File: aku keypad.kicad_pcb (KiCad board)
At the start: 2 copper layers, 47.6 x 46 mm, 19 parts, among them J1 USB_C_Receptacle_USB2.0, SW1 SW_Push, SW2 MX_SW_HS, SW3 MX_SW_HS, U1 SRV05-4, U2 ATmega32U2-M, Y1 Crystal_GND24_Small

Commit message: Added front ground fill
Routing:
- added copper zone on F.Cu, net GND
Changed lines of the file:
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@@
   (segment (start 47.7525 78.10125) (end 48.9025 76.95125) (width 0.25) (layer "B.Cu") (net 38))
   (segment (start 53.308597 72.549493) (end 52.851574 73.006516) (width 0.25) (layer "B.Cu") (net 38))
+  (zone (net 1) (net_name "GND") (layer "F.Cu") (hatch edge 0.508)
+    (connect_pads (clearance 0.508))
+    (min_thickness 0.254) (filled_areas_thickness no)
+    (fill yes (thermal_gap 0.508) (thermal_bridge_width 0.508))
+    (polygon
+      (pts
+        (xy 61.11875 39.6875)
+        (xy 79.375 39.6875)
+        (xy 79.375 78.58125)
+        (xy 31.75 78.58125)
+        (xy 31.75 39.6875)
+        (xy 50.00625 39.6875)
+        (xy 50.00625 32.54375)
+        (xy 61.11875 32.54375)
+      )
+    )
+  )
   (zone (net 1) (net_name "GND") (layer "B.Cu") (hatch edge 0.508)
     (connect_pads yes (clearance 0.508))

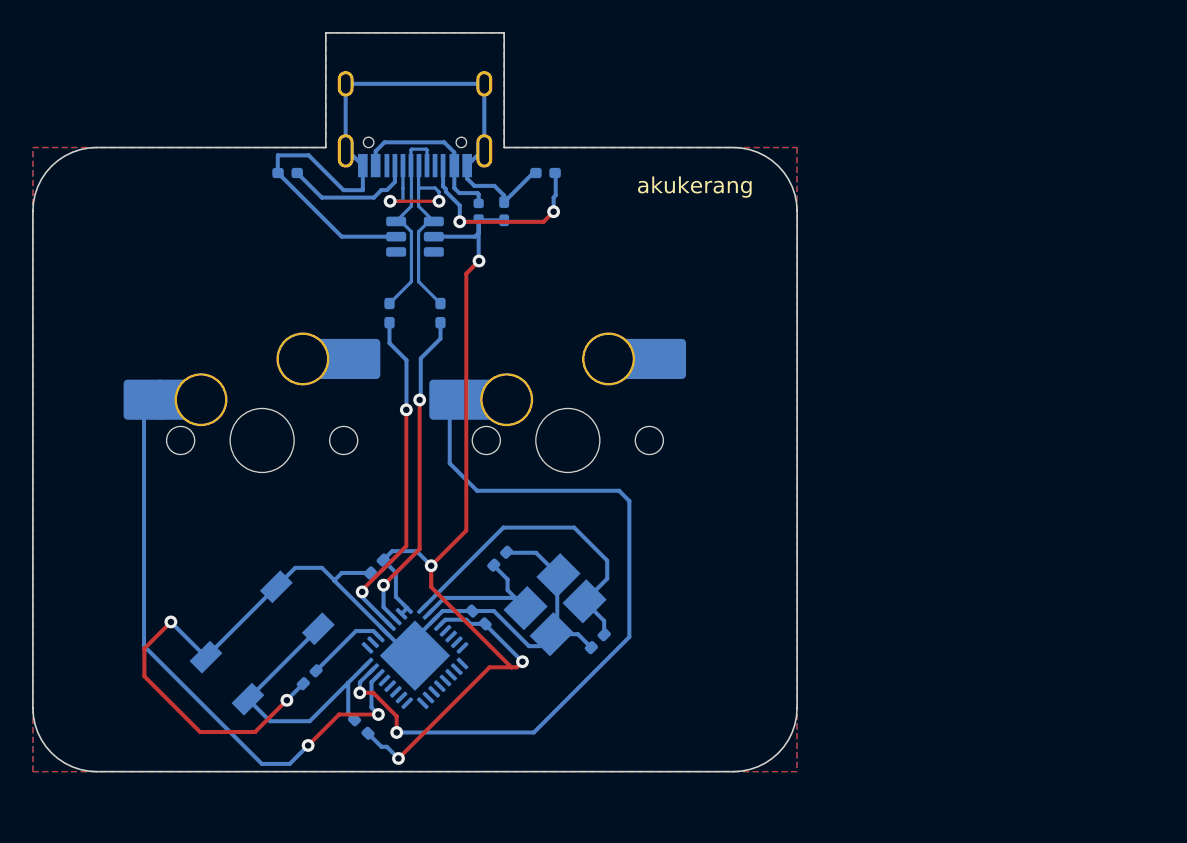
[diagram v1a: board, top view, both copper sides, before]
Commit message: redid routing on pcb
added type-c submodule, redid routing, changed usb components
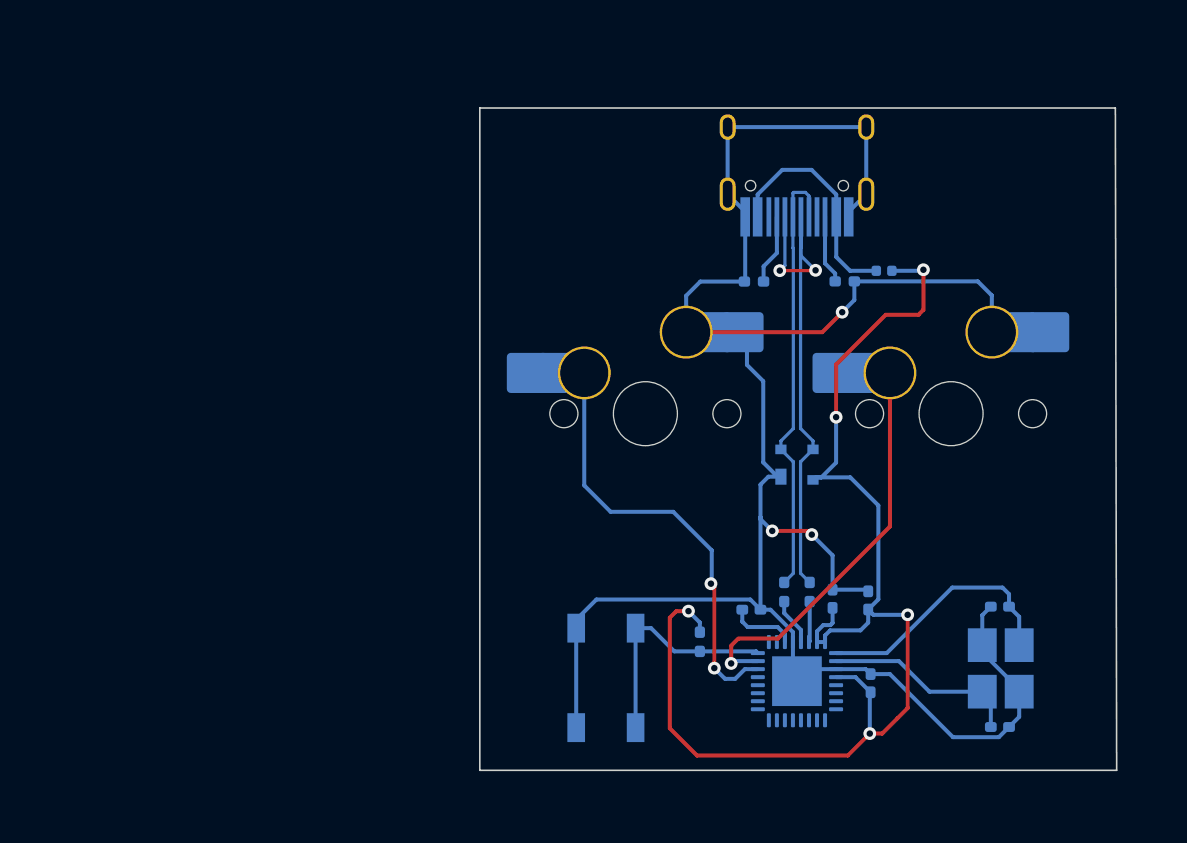
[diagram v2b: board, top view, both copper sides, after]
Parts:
- removed J1: USB_C_Receptacle_USB2.0, Connector_USB:USB_C_Receptacle_HRO_TYPE-C-31-M-12
- removed U1: SRV05-4, marbastlib-various:SOT-23-6-routable
- added D1: PRTR5V0U2X, Package_TO_SOT_SMD:SOT-143, B.Cu at (79.4, 59.5)
- added USB1: HRO-TYPE-C-31-M-12, Type-C:HRO-TYPE-C-31-M-12-HandSoldering, B.Cu at (79.4, 35.8)
- moved C6 37.2 mm to (84.0, 73.1)
- moved C2 32.9 mm to (92.0, 75.8), turned to 180 degrees
- moved R4 30.1 mm to (78.6, 67.4)
- moved R2 29.8 mm to (76.7, 48.0)
- moved R5 28.8 mm to (80.2, 67.4)
- moved C5 28.5 mm to (81.6, 67.8), turned to 90 degrees
- moved Y1 28.1 mm to (92.1, 72.2), turned to -90 degrees
- moved C3 27.8 mm to (76.5, 68.5), turned to 180 degrees
- moved F1 25.5 mm to (84.8, 47.4), turned to 0 degrees
- moved C1 25.2 mm to (92.0, 68.3), turned to 0 degrees
- moved C4 24.3 mm to (83.8, 67.9), turned to 90 degrees
- moved SW3 23.9 mm to (69.9, 56.3)
- moved SW2 23.9 mm to (89.0, 56.3)
- moved U2 23.9 mm to (79.4, 72.9), turned to 180 degrees
- moved R1 21.8 mm to (73.3, 70.5), turned to -90 degrees
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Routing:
- net GND: track 109.8 -> 140.5 mm, vias 2 -> 3
- net COL1: track 47.3 -> 28.9 mm, vias 2 -> 1
- net Net-(R4-Pad2): track 21.2 -> 2.95 mm, vias 2 -> 0
- net Net-(R5-Pad2): track 20.3 -> 2.54 mm, vias 2 -> 0
- net D-: track 17.4 -> 33.1 mm
- net D+: track 12.4 -> 27.6 mm
- net +5V: track 63.5 -> 78.1 mm, vias 4 -> 5
- net Net-(R3-Pad1): track 12.5 -> 4.28 mm, vias 2 -> 0
- net COL0: track 37.1 -> 30.9 mm
- net XTAL1: track 20.1 -> 16.1 mm
- net Net-(R2-Pad1): track 8.15 -> 4.37 mm
- net Net-(R1-Pad2): track 18.2 -> 14.5 mm
- net VCC: track 10.8 -> 14.3 mm
- net XTAL2: track 10.2 -> 12.3 mm
- net Net-(C3-Pad2): track 5.07 -> 4.21 mm
- removed copper zone on B.Cu, net GND
- removed copper zone on F.Cu, net GND
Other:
- board size 47.6 x 46 mm -> 39.7 x 41.3 mm
- board text removed: "akukerang"

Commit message: Added mounting holes
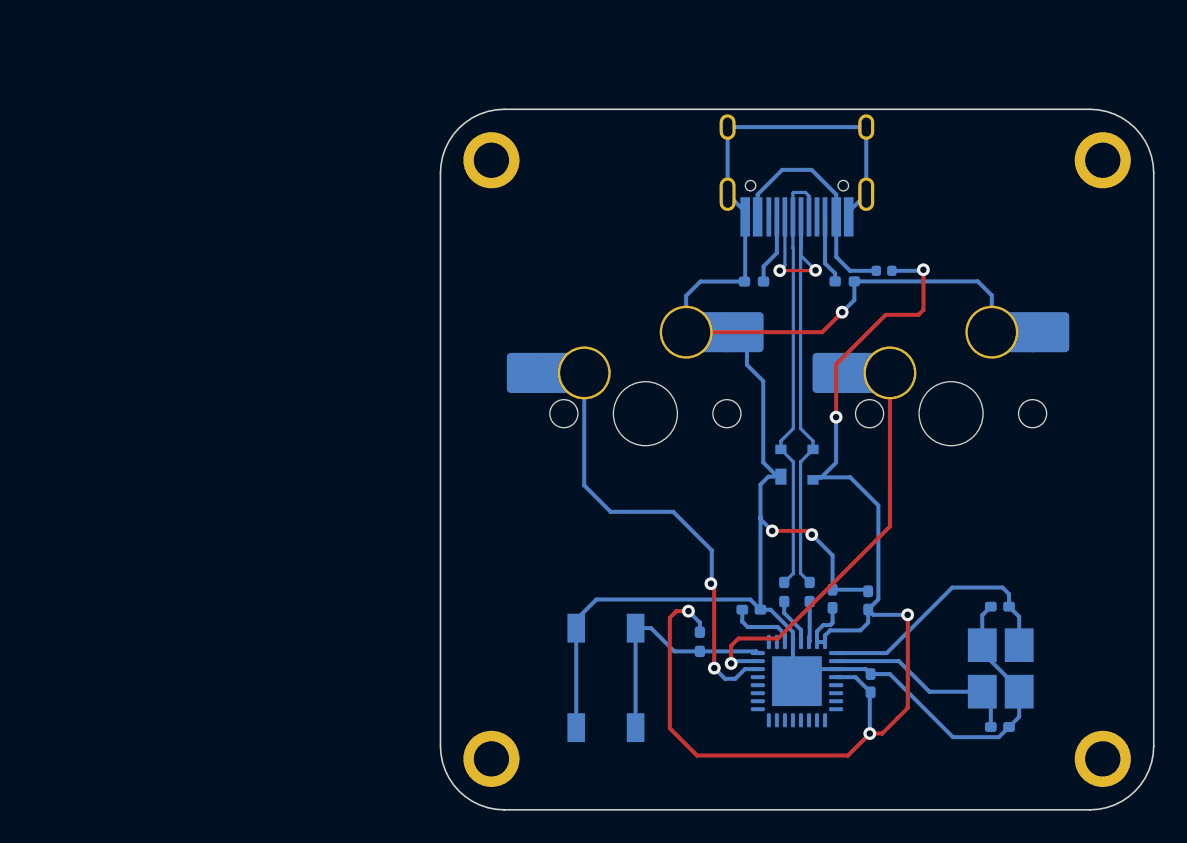
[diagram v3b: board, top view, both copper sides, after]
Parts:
- added H1: MountingHole, random-keyboard-parts:Generic-Mounthole, F.Cu at (60.3, 40.5)
- added H2: MountingHole, random-keyboard-parts:Generic-Mounthole, F.Cu at (98.4, 40.5)
- added H3: MountingHole, random-keyboard-parts:Generic-Mounthole, F.Cu at (60.3, 77.8)
- added H4: MountingHole, random-keyboard-parts:Generic-Mounthole, F.Cu at (98.4, 77.8)
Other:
- board size 39.7 x 41.3 mm -> 44.4 x 43.7 mm
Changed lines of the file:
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@@
   (net 35 "COL1")
   (net 36 "COL0")
+  (footprint "random-keyboard-parts:Generic-Mounthole" (layer "F.Cu")
+    (at 98.425 40.48125)
+    (property "Sheetfile" "aku keypad.kicad_sch")
+    (property "Sheetname" "")
+    (attr exclude_from_pos_files)
+    (fp_text reference "H2" (at 0 2) (layer "Dwgs.User")
+      (effects (font (size 1 1) (thickness 0.15)))
+    )
+    (fp_text value "MountingHole" (at 0 -2) (layer "Dwgs.User")
+      (effects (font (size 1 1) (thickness 0.15)))
+    )
+    (pad "1" thru_hole circle locked (at 0 0) (size 3.5 3.5) (drill 2.2) (layers *.Cu *.Mask))
+  )
+  (footprint "random-keyboard-parts:Generic-Mounthole" (layer "F.Cu")
+    (at 60.325 77.7875)
+    (property "Sheetfile" "aku keypad.kicad_sch")
+    (property "Sheetname" "")
+    (attr exclude_from_pos_files)
+    (fp_text reference "H3" (at 0 2) (layer "Dwgs.User")
+      (effects (font (size 1 1) (thickness 0.15)))
+    )
+    (fp_text value "MountingHole" (at 0 -2) (layer "Dwgs.User")
+      (effects (font (size 1 1) (thickness 0.15)))
+    )
+    (pad "1" thru_hole circle locked (at 0 0) (size 3.5 3.5) (drill 2.2) (layers *.Cu *.Mask))
+  )
+  (footprint "random-keyboard-parts:Generic-Mounthole" (layer "F.Cu")
+    (at 60.325 40.48125)
+    (property "Sheetfile" "aku keypad.kicad_sch")
+    (property "Sheetname" "")
+    (attr exclude_from_pos_files)
+    (fp_text reference "H1" (at 0 2) (layer "Dwgs.User")
+      (effects (font (size 1 1) (thickness 0.15)))
+    )
+    (fp_text value "MountingHole" (at 0 -2) (layer "Dwgs.User")
+      (effects (font (size 1 1) (thickness 0.15)))
+    )
+    (pad "1" thru_hole circle locked (at 0 0) (size 3.5 3.5) (drill 2.2) (layers *.Cu *.Mask))
+  )
+  (footprint "random-keyboard-parts:Generic-Mounthole" (layer "F.Cu")
+    (at 98.425 77.7875)
+    (property "Sheetfile" "aku keypad.kicad_sch")
+    (property "Sheetname" "")
+    (attr exclude_from_pos_files)
+    (fp_text reference "H4" (at 0 2) (layer "Dwgs.User")
+      (effects (font (size 1 1) (thickness 0.15)))
+    )
+    (fp_text value "MountingHole" (at 0 -2) (layer "Dwgs.User")
+      (effects (font (size 1 1) (thickness 0.15)))
+    )
+    (pad "1" thru_hole circle locked (at 0 0) (size 3.5 3.5) (drill 2.2) (layers *.Cu *.Mask))
+  )
   (footprint "Button_Switch_SMD:SW_SPST_SKQG_WithStem" (layer "B.Cu")
     (at 67.459644 72.74 -90)
@@
     )
   )
-  (gr_line (start 99.209644 37.225) (end 59.6025 37.225) (layer "Edge.Cuts") (width 0.1))
-  (gr_line (start 59.6025 78.5) (end 59.6025 37.225) (layer "Edge.Cuts") (width 0.1))
-  (gr_line (start 99.29 78.5) (end 59.6025 78.5) (layer "Edge.Cuts") (width 0.1))
-  (gr_line (start 99.29 78.5) (end 99.209644 37.225) (layer "Edge.Cuts") (width 0.1))
+  (gr_arc (start 61.11875 80.9625) (mid 58.31242 79.80008) (end 57.15 76.99375) (layer "Edge.Cuts") (width 0.1))
+  (gr_line (start 61.11875 37.30625) (end 97.63125 37.30625) (layer "Edge.Cuts") (width 0.1))
+  (gr_line (start 61.11875 80.9625) (end 97.63125 80.9625) (layer "Edge.Cuts") (width 0.1))
+  (gr_arc (start 97.63125 37.30625) (mid 100.43758 38.46867) (end 101.6 41.275) (layer "Edge.Cuts") (width 0.1))
+  (gr_line (start 57.15 41.275) (end 57.15 76.99375) (layer "Edge.Cuts") (width 0.1))
+  (gr_arc (start 101.6 76.99375) (mid 100.43758 79.80008) (end 97.63125 80.9625) (layer "Edge.Cuts") (width 0.1))
+  (gr_line (start 101.6 76.99375) (end 101.6 41.275) (layer "Edge.Cuts") (width 0.1))
+  (gr_arc (start 57.15 41.275) (mid 58.31242 38.46867) (end 61.11875 37.30625) (layer "Edge.Cuts") (width 0.1))
   (segment (start 82.185894 49.95) (end 80.940894 51.195) (width 0.25) (layer "F.Cu") (net 1))
   (segment (start 80.940894 51.195) (end 72.46125 51.195) (width 0.25) (layer "F.Cu") (net 1))

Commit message: more rerouting, added edge cuts around usb
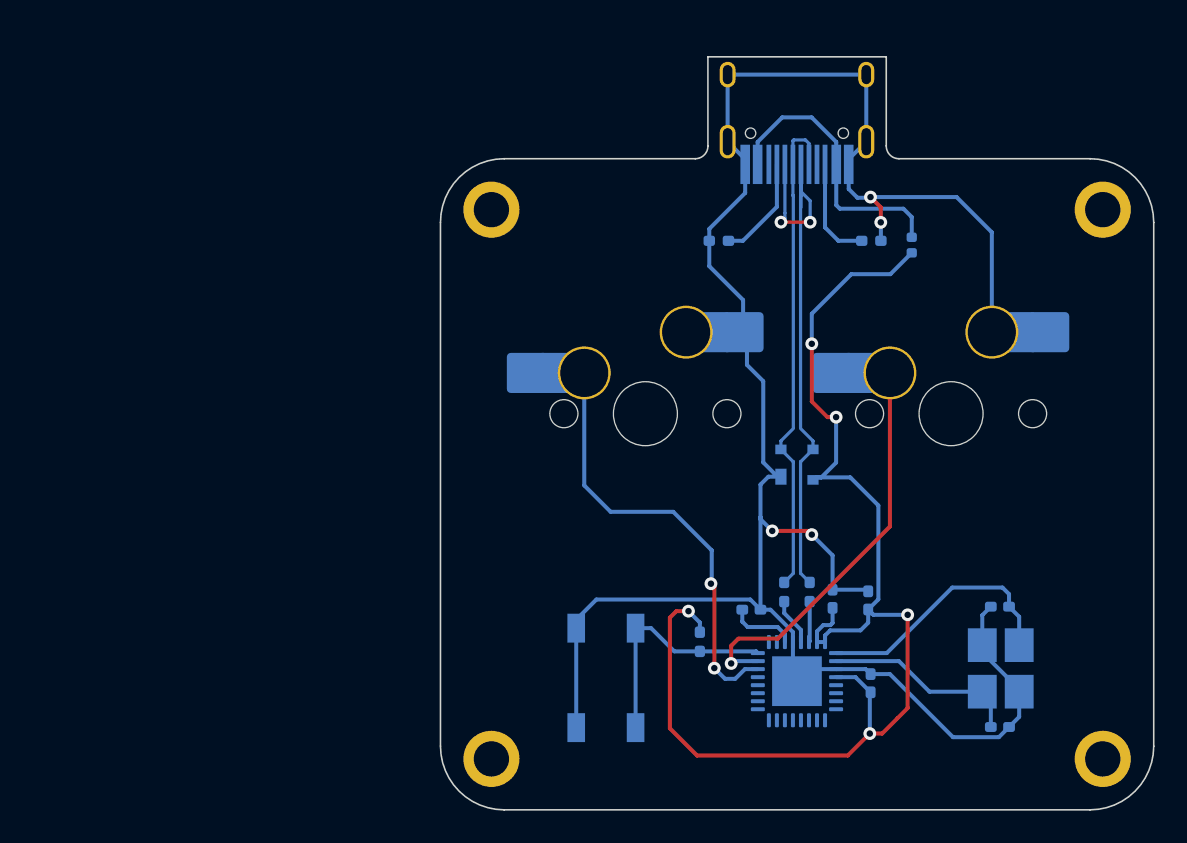
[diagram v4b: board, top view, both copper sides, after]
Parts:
- moved R2 3.35 mm to (74.5, 45.5)
- moved USB1 3.27 mm to (79.4, 32.5)
- moved H1 3.08 mm to (60.3, 43.6)
- moved H2 3.08 mm to (98.4, 43.6)
- moved R3 3.02 mm to (84.0, 45.5)
- moved F1 2.36 mm to (86.5, 45.8), turned to -90 degrees
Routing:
- net D-: track 33.1 -> 38.9 mm
- net VCC: track 14.3 -> 17.8 mm
- net D+: track 27.6 -> 30.8 mm
- net Net-(R3-Pad1): track 4.28 -> 6.56 mm
- net Net-(R2-Pad1): track 4.37 -> 6.54 mm
- net GND: track 140.5 -> 139.6 mm, vias 3 -> 4
- net +5V: track 78.1 -> 78.7 mm
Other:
- board size 44.4 x 43.7 mm -> 44.5 x 46.9 mm

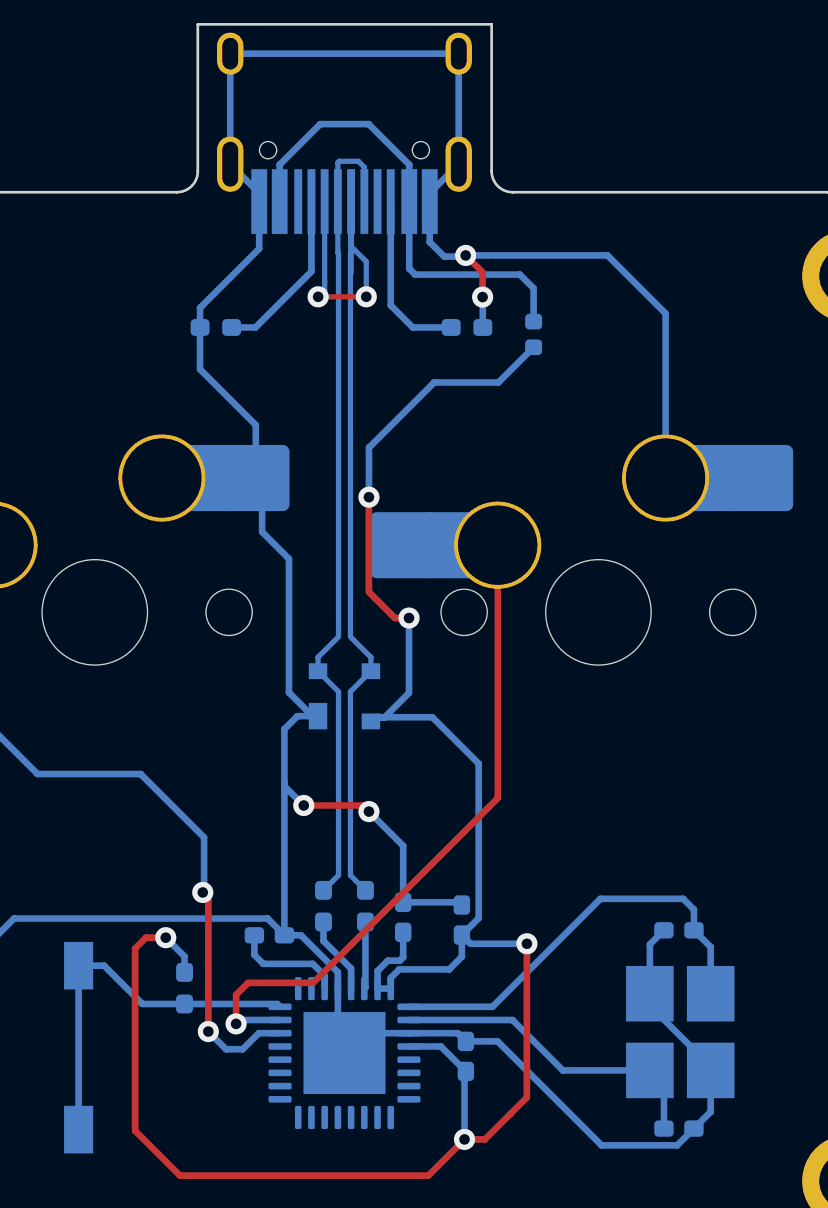
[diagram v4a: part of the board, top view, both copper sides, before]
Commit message: removed local files from repo
added cache and other things to gitignore
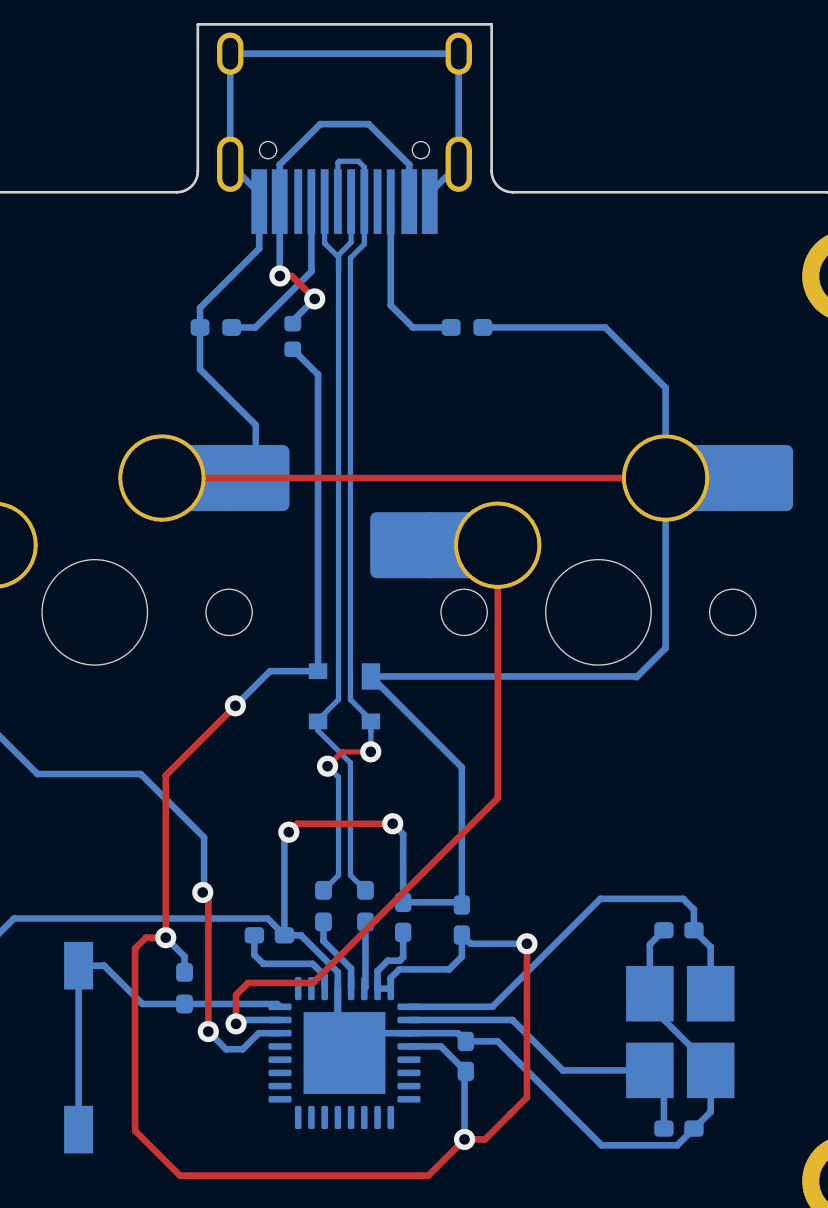
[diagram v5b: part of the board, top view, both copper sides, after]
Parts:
- moved F1 9.11 mm to (77.4, 45.8)
- turned D1 to 180 degrees
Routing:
- net GND: track 139.6 -> 159.8 mm, vias 4 -> 2
- net D-: track 38.9 -> 30.2 mm, vias 2 -> 0
- net +5V: track 78.7 -> 73.8 mm, vias 5 -> 4
- net VCC: track 17.8 -> 14.7 mm, vias 0 -> 2
- net D+: track 30.8 -> 32.2 mm, vias 0 -> 2
